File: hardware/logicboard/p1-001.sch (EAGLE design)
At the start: 23 parts, among them IC1 74LS07N

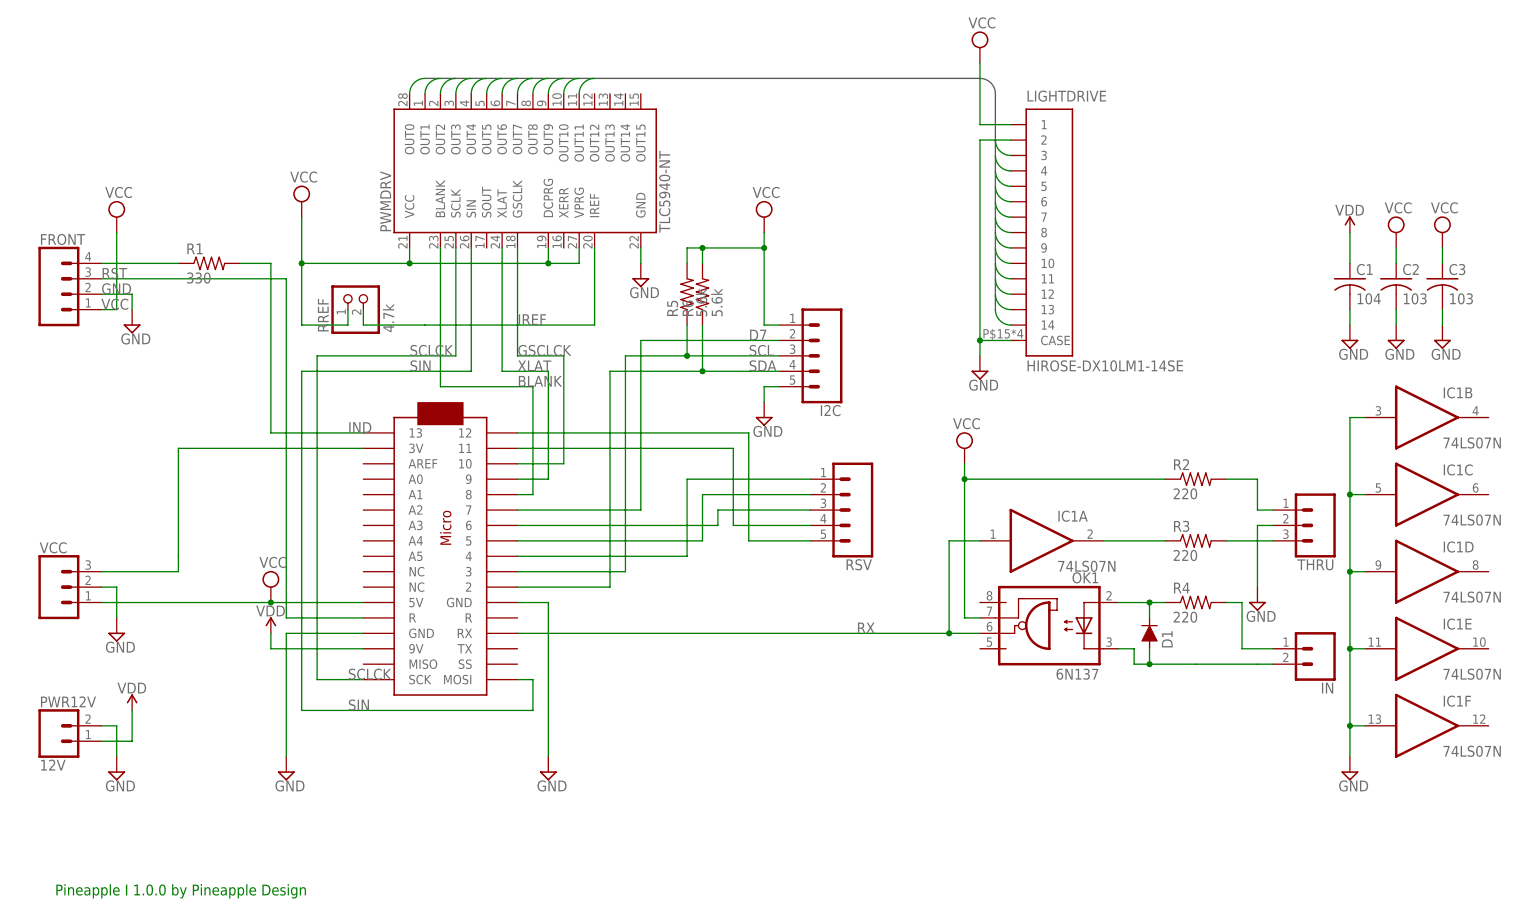
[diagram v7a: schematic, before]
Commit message: New analog/reserve ports.
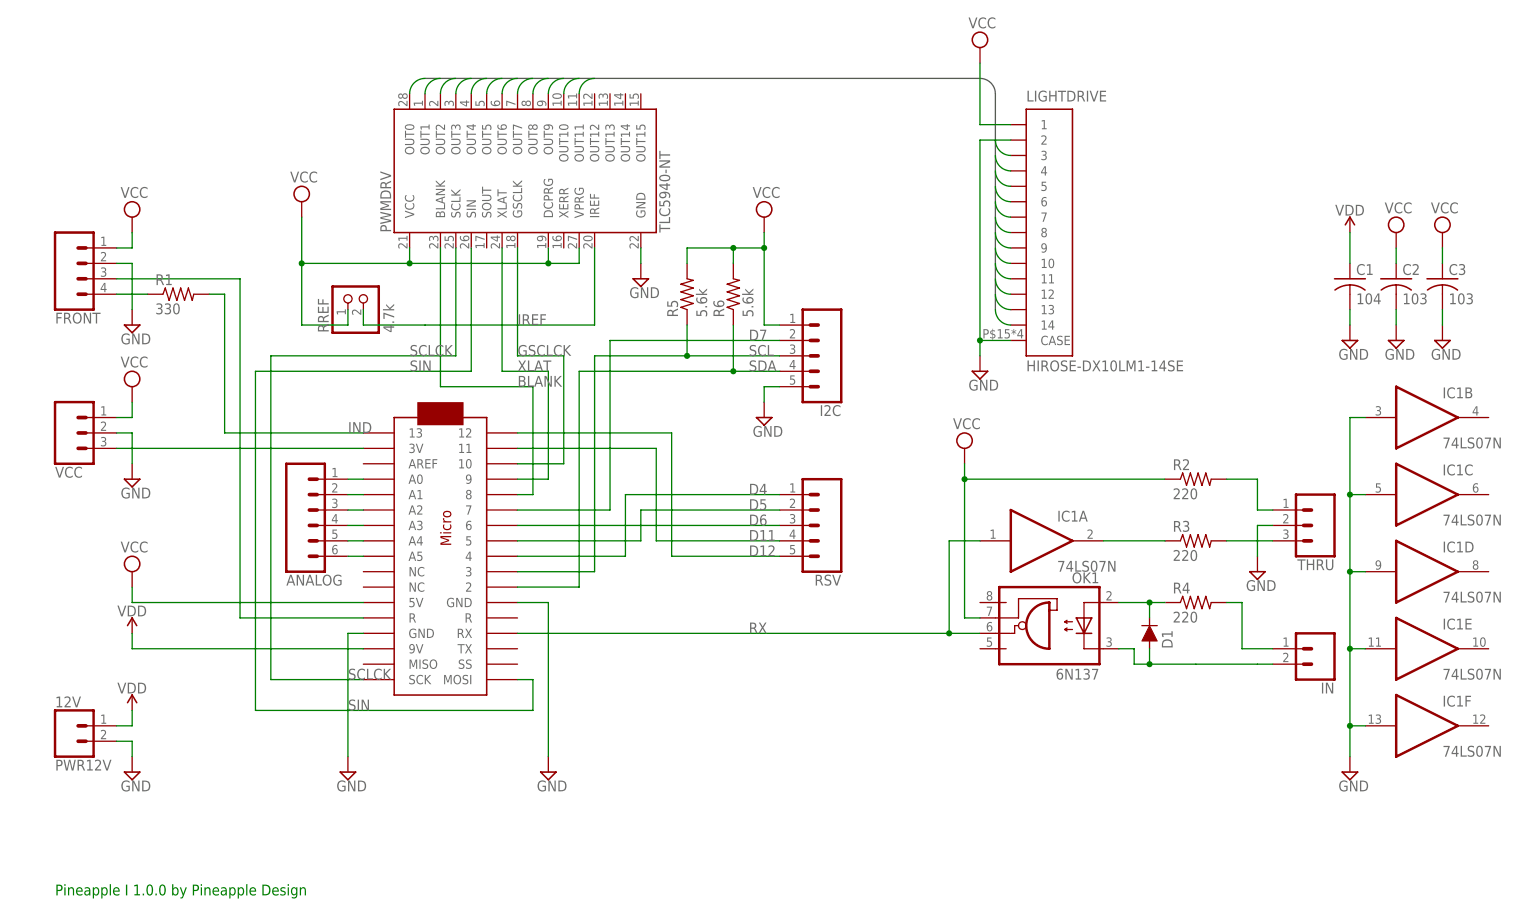
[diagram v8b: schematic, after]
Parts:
- added ANALOG: (no value), SparkFun-Connectors:CONN_061.27MM
- RSV: device SparkFun-Connectors:CONN_05JST-VERT -> SparkFun-Connectors:CONN_051.27MM
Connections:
- net N$1 renamed D4
- net N$4 renamed D5
- net N$6 renamed D6
- net N$7 renamed D11
- net N$8 renamed D12
- new net N$10: ANALOG.2, U$1.A1
- new net N$11: ANALOG.3, U$1.A2
- new net N$12: ANALOG.4, U$1.A3
- new net N$13: ANALOG.5, U$1.A4
- new net N$14: ANALOG.6, U$1.A5
- new net N$9: ANALOG.1, U$1.A0
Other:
- moved on the sheet: FRONT, PWR12V, R1, R6, RSV, VCC
